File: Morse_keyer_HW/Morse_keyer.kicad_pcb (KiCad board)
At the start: 2 copper layers, 65 x 30 mm, 36 parts, among them P1 CONN_01X05, P2 CONN_01X02, SW1 SWITCH, SW2 SWITCH, SW3 SWITCH, SW4 SWITCH, SW5 SWITCH, SW6 SWITCH, U1 EFM32PG1B200F256

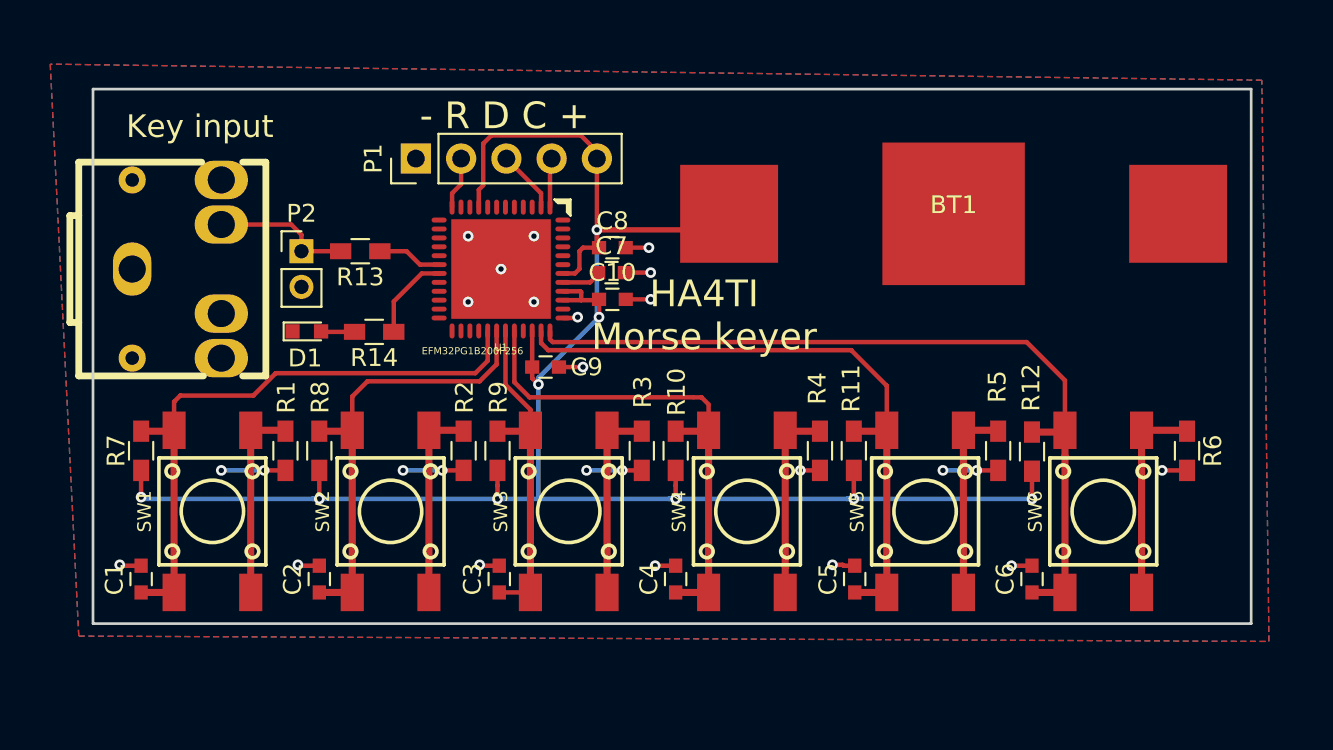
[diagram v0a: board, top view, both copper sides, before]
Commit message: Changed chip to QFN32 EFR32MG1
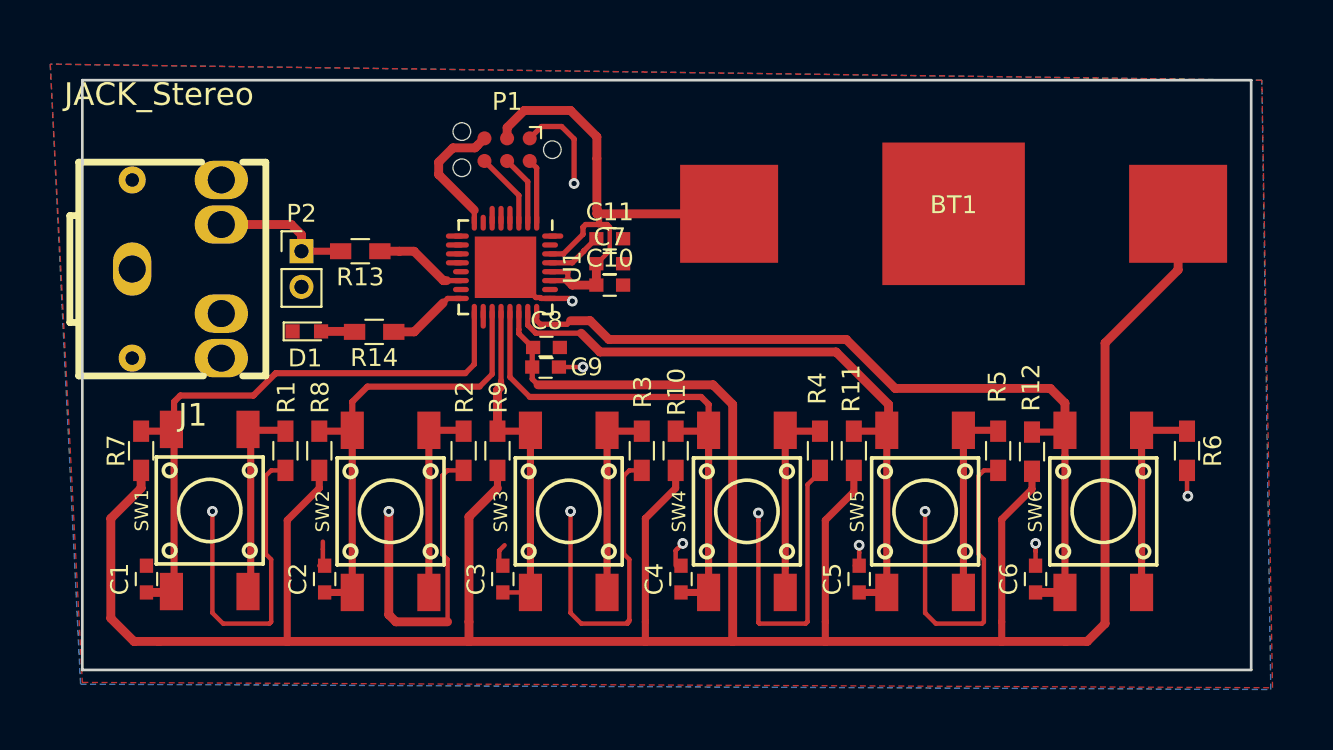
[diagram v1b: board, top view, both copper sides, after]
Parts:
- removed Key input: JACK_Stereo, Tibi lib KiCAD:AudioJack3.5mm_stereo
- added C11: 100n, Capacitors_SMD:C_0603, F.Cu at (64.3, -20.3)
- added J1: JACK_Stereo, Tibi lib KiCAD:AudioJack3.5mm_stereo, F.Cu at (37.5, -18.6)
- P1: value CONN_01X05 -> TagConnect; footprint Pin_Headers:Pin_Header_Straight_1x05_Pitch2.54mm -> Connect:Tag-Connect_TC2030-IDC-NL
- U1: value EFM32PG1B200F256 -> EFR32MG1_QFN32; footprint Tibi lib KiCAD:QFN48 -> Tibi lib KiCAD:QFN-32-1EP_5x5mm_Pitch0.5mm
- moved C8 6.71 mm to (60.8, -14.2)
- moved P1 5.14 mm to (58.5, -25.3), turned to 180 degrees
- moved C10 0.81 mm to (64.3, -17.7)
- moved C7 0.51 mm to (64.3, -18.9)
- moved C1 0.30 mm to (38.3, -1.20)
- moved C2 0.30 mm to (48.3, -1.20)
- moved C4 0.30 mm to (68.3, -1.20)
- moved U1 0.27 mm to (58.5, -18.7), turned to 270 degrees
- moved C5 0.25 mm to (78.3, -1.20)
- moved C6 0.20 mm to (88.2, -1.20)
- moved C3 0.20 mm to (58.3, -1.20)
- moved SW1 0.16 mm to (41.9, -5.05)
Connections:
- BT1 pad 1: +3V3 -> +BATT
- C10 pad 1: +3V3 -> +BATT
- C7 pad 1: Net-(C7-Pad1) -> +BATT
- C8 pad 1: +3V3 -> +BATT
- C9 pad 1: +3V3 -> +BATT
- P1 pad 2: /~RESET -> /SWC
- P1 pad 3: /SWD -> +BATT
- P1 pad 4: /SWC -> /SWD
- P1 pad 5: +3V3 -> /~RESET
- R10 pad 2: +3V3 -> +BATT
- R11 pad 2: +3V3 -> +BATT
- R12 pad 2: +3V3 -> +BATT
- R7 pad 2: +3V3 -> +BATT
- R8 pad 2: +3V3 -> +BATT
- R9 pad 2: +3V3 -> +BATT
- U1 pad 12: /~RESET -> Net-(U1-Pad12)
- U1 pad 14: Net-(U1-Pad14) -> Net-(R13-Pad1)
- U1 pad 16: Net-(U1-Pad16) -> Net-(R14-Pad1)
- U1 pad 17: Net-(U1-Pad17) -> /Button1
- U1 pad 18: Net-(R13-Pad1) -> Net-(U1-Pad18)
- U1 pad 19: Net-(R14-Pad1) -> /Button2
- U1 pad 20: Net-(U1-Pad20) -> /Button3
- U1 pad 21: Net-(U1-Pad21) -> /Button4
- U1 pad 22: Net-(U1-Pad22) -> +BATT
- U1 pad 23: Net-(U1-Pad23) -> /Button5
- U1 pad 24: Net-(U1-Pad24) -> /Button6
- U1 pad 25: Net-(U1-Pad25) -> GND
- U1 pad 27: Net-(U1-Pad27) -> +BATT
- U1 pad 28: Net-(U1-Pad28) -> +BATT
- U1 pad 29: /Button1 -> /Decouple
- U1 pad 3: Net-(U1-Pad3) -> /SWO
- U1 pad 30: /Button2 -> +BATT
- U1 pad 31: /Button3 -> Net-(U1-Pad31)
- U1 pad 32: /Button4 -> Net-(U1-Pad32)
- U1 pad 33: Net-(U1-Pad33) -> GND
- U1 pad 8: Net-(U1-Pad8) -> /~RESET
- U1 pad 9: +3V3 -> Net-(U1-Pad9)
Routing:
- net +BATT: track 0.00 -> 204.4 mm
- net +3V3: track 112.4 -> 0.00 mm, vias 9 -> 0
- net GND: track 29.2 -> 111.6 mm, vias 26 -> 12
- net /Key: track 8.36 -> 13.1 mm
- net /SWO: track 0.00 -> 4.26 mm
- net /Button6: track 46.0 -> 50.2 mm
- net /~RESET: track 3.34 -> 7.35 mm
- net /Decouple: track 0.00 -> 3.24 mm
- net Net-(C7-Pad1): track 2.31 -> 0.00 mm
- net /Button5: track 36.3 -> 38.5 mm
- net /Button4: track 28.6 -> 30.5 mm
- net Net-(R13-Pad1): track 3.64 -> 5.23 mm
- net /Button2: track 25.4 -> 26.3 mm
- net Net-(U1-Pad6): track 0.00 -> 0.80 mm
- net Net-(U1-Pad5): track 0.00 -> 0.80 mm
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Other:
- board size 65 x 30 mm -> 65.6 x 33.1 mm
- board text removed: "- R D C +"

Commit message: Changed to QFN32 package EFR32MG1
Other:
- board size 65.6 x 33.1 mm -> 69.6 x 37.2 mm
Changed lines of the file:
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@@
     (effects (font (size 1.5 1.5) (thickness 0.3)))
   )
-  (gr_line (start 34.7 -29.2) (end 34.7 3.9) (layer Edge.Cuts) (width 0.15))
-  (gr_line (start 100.3 -29.2) (end 34.7 -29.2) (layer Edge.Cuts) (width 0.15))
-  (gr_line (start 100.3 3.9) (end 100.3 -29.2) (layer Edge.Cuts) (width 0.15))
-  (gr_line (start 34.7 3.9) (end 100.3 3.9) (layer Edge.Cuts) (width 0.15))
+  (gr_line (start 32.7 -31.2) (end 32.7 6) (layer Edge.Cuts) (width 0.15))
+  (gr_line (start 102.3 -31.2) (end 32.7 -31.2) (layer Edge.Cuts) (width 0.15))
+  (gr_line (start 102.3 6) (end 102.3 -31.2) (layer Edge.Cuts) (width 0.15))
+  (gr_line (start 32.7 6) (end 102.3 6) (layer Edge.Cuts) (width 0.15))
   (segment (start 38.3 -0.45) (end 39.65 -0.45) (width 0.5) (layer F.Cu) (net 1))
   (segment (start 39.65 -0.45) (end 39.7 -0.5) (width 0.5) (layer F.Cu) (net 1))
@@
     (polygon
       (pts
-        (xy 100.9 -29.2) (xy 32.9 -30.1) (xy 34.7 4.6) (xy 101.5 4.9)
+        (xy 102.8 -31.6) (xy 32.2 -31.5) (xy 32.3 6.3) (xy 102.9 6.3)
       )
     )
@@
     (polygon
       (pts
-        (xy 100.9 -29.2) (xy 32.9 -30.1) (xy 34.6 4.7) (xy 101.4 5)
+        (xy 102.8 -31.7) (xy 32.2 -31.5) (xy 32.3 6.3) (xy 102.9 6.4)
       )
     )
